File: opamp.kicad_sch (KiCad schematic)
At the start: 22 parts, among them J1 Conn_01x06, Q1 BFP420, Q10 BFP420, Q11 BFP420, Q2 BFP420, Q3 BFP520, Q4 BFP520, Q5 BFP520, Q6 BFP520, Q7 BFP520, Q8 BFP420, Q9 BFP420

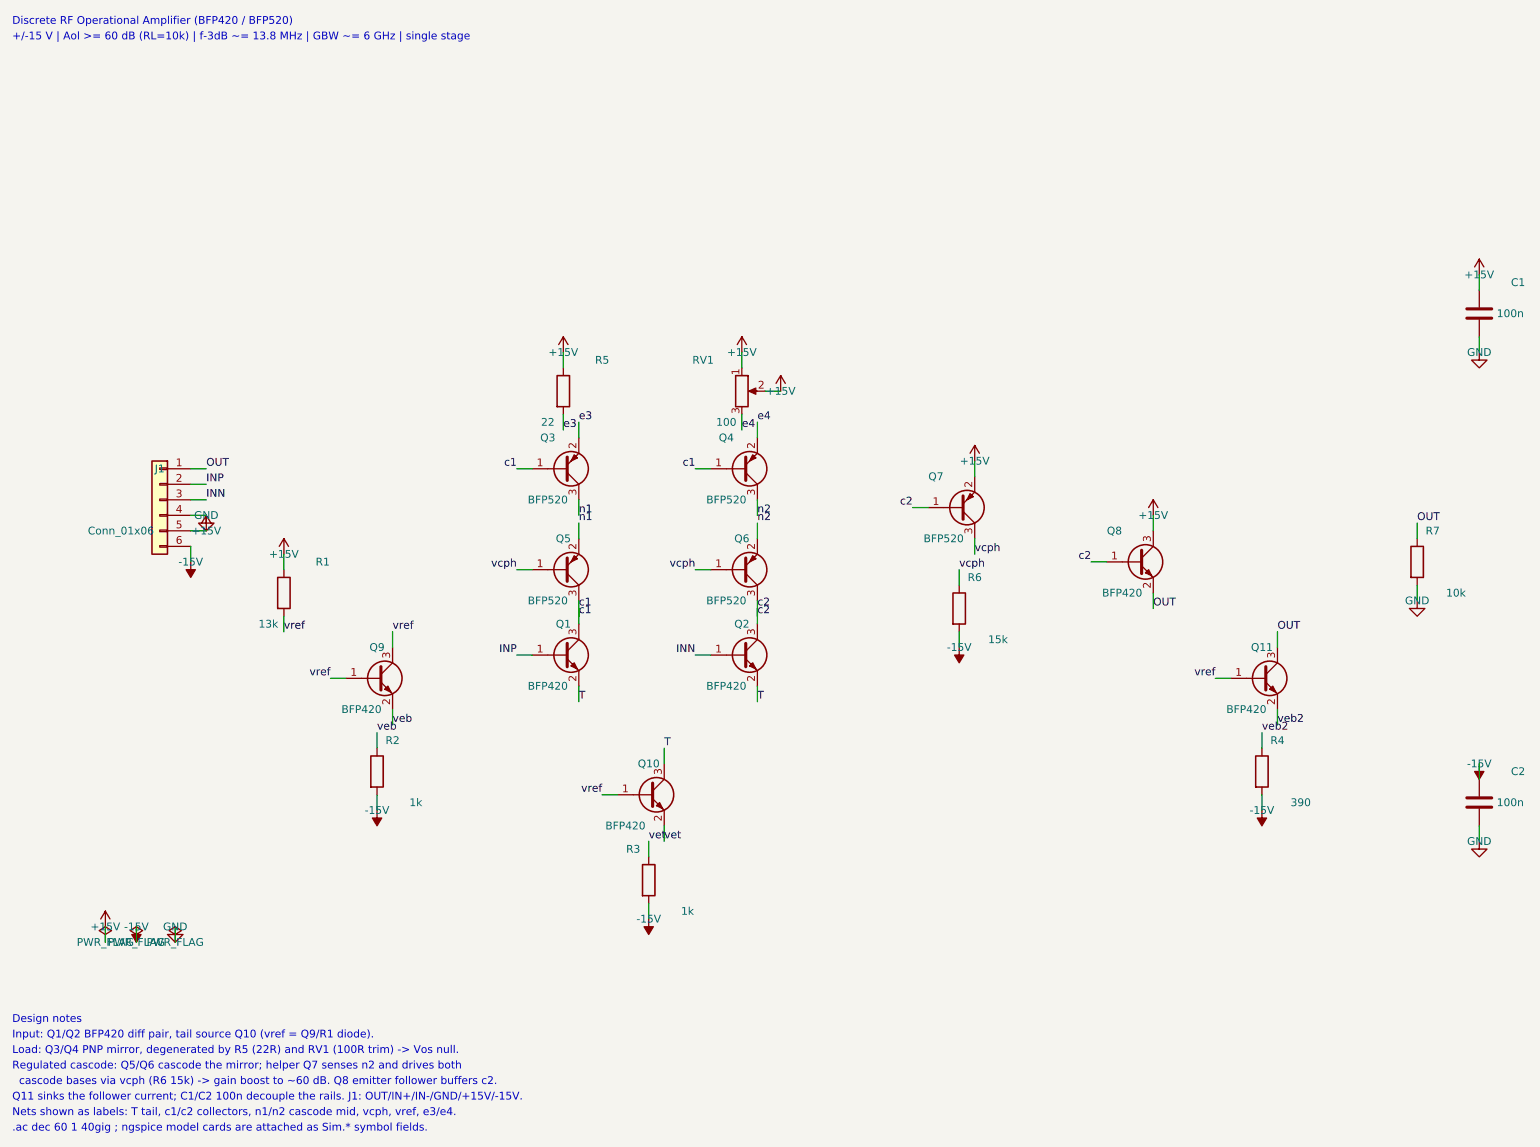
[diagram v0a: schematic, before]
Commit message: Fix Rev-C schematic wiring, replace offset trimmer with fixed R8
The schematic generator drew a wire-based Rev-C (BFP420/BFP520) design, but
its coordinates were off-grid for the J1 connector stubs and the C1/C2
decoupling power symbols, so those pins were silently unconnected.  kicad-cli
reported 36 ERC violations (16 errors); it is now 0.  The earlier "ERC clean"
claim came from a tool that did not catch it.

- gen_sch_rf.py: land the J1 stubs on the real pin coordinates (x 45.08->45.72,
  y +0.17) and place the C1/C2 power symbols on the capacitor pins (x 255->254).
- Replace the RV1 100R offset trimmer with a fixed R8 = 54.9R (E96) that nulls
  the amplifier's *systematic* input offset (~16 mV, from the input pair's
  VAF-limited collector-voltage difference plus the saturated reference-side
  cascode).  No trimmer is needed; cost is ~1.4 dB of Aol.
- Align R1/Rbias to 13.7k in the schematic and README (the sim, which produced
  every published number, already used 13.7k).
- Update README sections 5d/5e/6 and the component table; quote the shipped
  model's measured point (Aol 58.8 dB, f-3dB 12.8 MHz, GBW 6.08 GHz, PM 66.3,
  Vos ~0 at RL = 10k).
- Track the README figure in artifacts/ and add its renderer
  (sim/render_openloop_bode.py) since sim/*.png is gitignored.
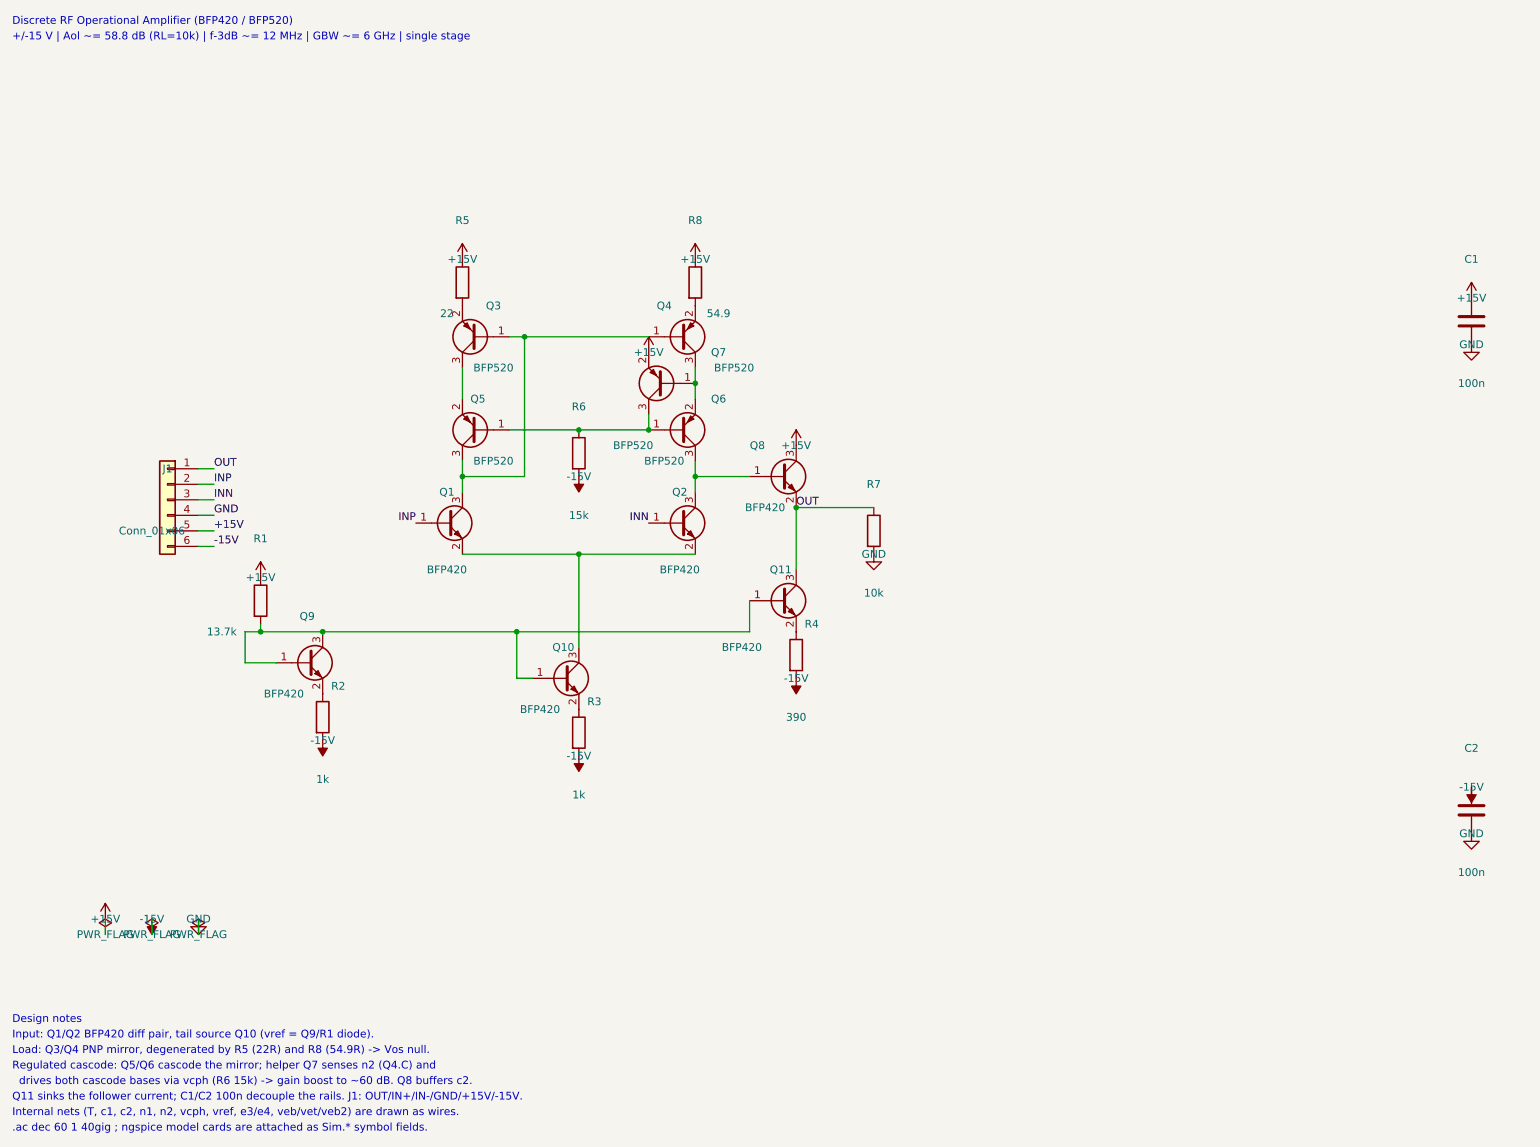
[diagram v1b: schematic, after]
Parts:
- removed RV1: 100, Potentiometer_SMD:Potentiometer_Bourns_3214W_Vertical, symbol Device:R_Potentiometer
- added R8: 54.9, Resistor_SMD:R_0603_1608Metric, symbol Device:R
- R1: value 13k -> 13.7k
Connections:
- net +15V: now also R8.1
- net T: no longer names the net of Q1.2 (E), Q10.3 (C), Q2.2 (E)
- net c1: no longer names the net of Q1.3 (C), Q3.1 (B), Q4.1 (B), Q5.3 (C)
- net c2: no longer names the net of Q2.3 (C), Q6.3 (C), Q8.1 (B)
- net c2: no longer Q7.1 (B)
- net e3: no longer names the net of Q3.2 (E), R5.2
- net e4: no longer names the net of Q4.2 (E)
- net e4: now also R8.2
- net n1: no longer names the net of Q3.3 (C), Q5.2 (E)
- net n2: no longer names the net of Q4.3 (C), Q6.2 (E)
- net n2: now also Q7.1 (B)
- net vcph: no longer names the net of Q5.1 (B), Q6.1 (B), Q7.3 (C), R6.1
- net veb: no longer names the net of Q9.2 (E), R2.1
- net veb2: no longer names the net of Q11.2 (E), R4.1
- net vet: no longer names the net of Q10.2 (E), R3.1
- net vref: no longer names the net of Q10.1 (B), Q11.1 (B), Q9.1 (B), Q9.3 (C), R1.2
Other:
- note added: "+/-15 V | Aol ~= 58.8 dB (RL=10k) | f-3dB ~= 12 MHz | GBW ~= 6 GHz | single stage"
- note added: "Internal nets (T, c1, c2, n1, n2, vcph, vref, e3/e4, veb/vet/veb2) are drawn as wires."
- note added: "Load: Q3/Q4 PNP mirror, degenerated by R5 (22R) and R8 (54.9R) -> Vos null."
- note added: "Regulated cascode: Q5/Q6 cascode the mirror; helper Q7 senses n2 (Q4.C) and"
- note added: "drives both cascode bases via vcph (R6 15k) -> gain boost to ~60 dB. Q8 buffers c2."
- note removed: "+/-15 V | Aol >= 60 dB (RL=10k) | f-3dB ~= 13.8 MHz | GBW ~= 6 GHz | single stage"
- note removed: "Load: Q3/Q4 PNP mirror, degenerated by R5 (22R) and RV1 (100R trim) -> Vos null."
- note removed: "Nets shown as labels: T tail, c1/c2 collectors, n1/n2 cascode mid, vcph, vref, e3/e4."
- note removed: "Regulated cascode: Q5/Q6 cascode the mirror; helper Q7 senses n2 and drives both"
- note removed: "cascode bases via vcph (R6 15k) -> gain boost to ~60 dB. Q8 emitter follower buffers c2."
